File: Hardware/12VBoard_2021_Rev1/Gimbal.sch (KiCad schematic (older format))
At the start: 33 parts, among them Q6 CSD18537NQ5A, Q7 CSD18531Q5A, Q8 IRLML2060, U12 LM5116, U13 INA198, U3 LT1910

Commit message: found Big inductors
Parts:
- L8: value 6.8uH 1.5m -> 10uH; footprint MRDT_12VoltBoard:IND_SER2915L-682KL -> Inductor_THT:L_Radial_D27.9mm_P20.07mm_Vishay_IHB-3
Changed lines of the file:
@@
 AR Path="/5F74F36B/5FB68F3E/5FB7D727" Ref="L?"  Part="1"
 F 0 "L8" V 1600 3450 50  0000 C CNN
-F 1 "6.8uH 1.5m" V 1500 3450 50  0000 C CNN
-F 2 "MRDT_12VoltBoard:IND_SER2915L-682KL" H 1450 3550 50  0001 C CNN
+F 1 "10uH" V 1500 3450 50  0000 C CNN
+F 2 "Inductor_THT:L_Radial_D27.9mm_P20.07mm_Vishay_IHB-3" H 1450 3550 50  0001 C CNN
 F 3 "~" H 1450 3550 50  0001 C CNN
 	1    1450 3550

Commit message: Added all logic circuits for high current
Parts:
- R33: footprint Resistor_SMD:R_2512_6332Metric_Pad1.52x3.35mm_HandSolder -> Package_TO_SOT_THT:TO-126-2_Vertical
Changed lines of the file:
@@
 F 0 "R33" V 3193 3550 50  0000 C CNN
 F 1 "50m" V 3284 3550 50  0000 C CNN
-F 2 "Resistor_SMD:R_2512_6332Metric_Pad1.52x3.35mm_HandSolder" V 3330 3550 50  0001 C CNN
+F 2 "Package_TO_SOT_THT:TO-126-2_Vertical" V 3330 3550 50  0001 C CNN
 F 3 "~" H 3400 3550 50  0001 C CNN
 	1    3400 3550

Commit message: changed to big bucks
changed to the bucks used in Master due to a realization in the inductor sizing for the LM5116. It would be much bigger than previous years.
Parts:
- removed C33, C36: 100nF, Capacitor_SMD:C_0603_1608Metric_Pad1.05x0.95mm_HandSolder, symbol Device:C_Small
- removed C34: 2.2uF, Capacitor_SMD:C_0603_1608Metric_Pad1.05x0.95mm_HandSolder, symbol Device:C_Small
- removed C35: 1uF, Capacitor_SMD:C_0603_1608Metric_Pad1.05x0.95mm_HandSolder, symbol Device:C_Small
- removed C37, C40: 100uF, Capacitor_THT:CP_Radial_D6.3mm_P2.50mm, symbol Device:CP1_Small
- removed C38: 10pF, Capacitor_SMD:C_0603_1608Metric_Pad1.05x0.95mm_HandSolder, symbol Device:C_Small
- removed C39: 120pF, Capacitor_SMD:C_0603_1608Metric_Pad1.05x0.95mm_HandSolder, symbol Device:C_Small
- removed C41: 470pF, Capacitor_SMD:C_0603_1608Metric_Pad1.05x0.95mm_HandSolder, symbol Device:C_Small
- removed C42: 33nF, Capacitor_SMD:C_0603_1608Metric_Pad1.05x0.95mm_HandSolder, symbol Device:C_Small
- removed D17: 1.25V 250mA, Diode_SMD:D_SOD-323_HandSoldering, symbol Device:D_Small
- removed L8: 10uH, Inductor_THT:L_Radial_D27.9mm_P20.07mm_Vishay_IHB-3, symbol Device:L_Small
- removed Q6: CSD18537NQ5A, Package_SON:VSONP-8-1EP_5x6_P1.27mm, symbol 12VBoard_2021_Rev1-rescue:CSD18537NQ5A
- removed Q7: CSD18531Q5A, Package_SON:VSONP-8-1EP_5x6_P1.27mm, symbol 12VBoard_2021_Rev1-rescue:CSD18531Q5A
- removed R27: 5m, Resistor_SMD:R_0603_1608Metric_Pad1.05x0.95mm_HandSolder, symbol Device:R_Small
- removed R28: 36.5K, Resistor_SMD:R_0603_1608Metric_Pad1.05x0.95mm_HandSolder, symbol Device:R_Small
- removed R29: 2.26K, Resistor_SMD:R_0603_1608Metric_Pad1.05x0.95mm_HandSolder, symbol Device:R_Small
- removed R30: 86.6K, Resistor_SMD:R_0603_1608Metric_Pad1.05x0.95mm_HandSolder, symbol Device:R_Small
- removed R31: 9.76k, Resistor_SMD:R_0603_1608Metric_Pad1.05x0.95mm_HandSolder, symbol Device:R_Small
- removed R32: 261K, Resistor_SMD:R_0603_1608Metric_Pad1.05x0.95mm_HandSolder, symbol Device:R_Small
- removed U12: LM5116, Package_SO:TSSOP-20_4.4x6.5mm_P0.65mm, symbol 12VBoard_2021_Rev1-rescue:LM5116
- added C?: 0.1uF, Capacitor_SMD:C_0603_1608Metric_Pad1.05x0.95mm_HandSolder, symbol Device:C_Small
- added C?: 10uF, Capacitor_THT:CP_Radial_D5.0mm_P2.00mm, symbol Device:CP1_Small
- added R?: 0.01, Resistor_SMD:R_0603_1608Metric_Pad1.05x0.95mm_HandSolder, symbol Device:R
- added R?: 5.1K, Resistor_SMD:R_0603_1608Metric_Pad1.05x0.95mm_HandSolder, symbol Device:R
- added U?: LT1910, Package_SO:SOIC-8-N7_3.9x4.9mm_P1.27mm, symbol MRDT_ICs:LT1910
- added U?: FDS66900AS, symbol 12VBoard_2021_Rev1:FDS66900AS
- F3: value 5AMP -> 5A
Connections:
- net labels added: 12Actuation, 12V5AON
- net labels removed: AGNDPGND, COMPFB, CS, CSGDEMB, HB, HO, LO, PackVoltage, SW, VCC, VOUTVCCX
- wire segments 167 -> 81
- no-connect marks 1 -> 0
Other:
- moved on the sheet: D18, F3, R33, R34, TP7, U13

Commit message: Started work on updated layout
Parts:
- added D15: Aux Mount Acuation Gree, Diode_SMD:D_0603_1608Metric_Pad1.05x0.95mm_HandSolder, symbol Device:LED
- added R22: 1.2k, Resistor_SMD:R_0603_1608Metric_Pad1.05x0.95mm_HandSolder, symbol Device:R
- U18: renamed from U?; footprint (none) -> Package_SO:SOIC-8_3.9x4.9mm_P1.27mm
- gave numbers to parts that had none: 5
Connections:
- wire segments 81 -> 82
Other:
- note removed: "Green"
- moved on the sheet: D18, R34
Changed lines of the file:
@@
 $EndDescr
-$Comp
-L Device:R R?
-U 1 1 5F98969B
-P 3975 2950
-AR Path="/5F74F36B/5F821EB2/5F98969B" Ref="R?"  Part="1"
-AR Path="/5F74F36B/5F8222BE/5F98969B" Ref="R?"  Part="1"
-AR Path="/5F74F36B/5F971CD6/5F98969B" Ref="R34"  Part="1"
-AR Path="/5F74F36B/5FB68F3E/5F98969B" Ref="R?"  Part="1"
-F 0 "R34" H 4025 2950 50  0000 L CNN
-F 1 "1.2k" V 3975 2880 39  0000 L CNN
-F 2 "Resistor_SMD:R_0603_1608Metric_Pad1.05x0.95mm_HandSolder" V 3905 2950 50  0001 C CNN
-F 3 "~" H 3975 2950 50  0001 C CNN
-	1    3975 2950
-	1    0    0    -1
-$EndComp
-$Comp
-L power:GND #PWR?
-U 1 1 5F9896A1
-P 3975 3600
-AR Path="/5F74F36B/5F821EB2/5F9896A1" Ref="#PWR?"  Part="1"
-AR Path="/5F74F36B/5F8222BE/5F9896A1" Ref="#PWR?"  Part="1"
-AR Path="/5F74F36B/5F971CD6/5F9896A1" Ref="#PWR078"  Part="1"
-AR Path="/5F74F36B/5FB68F3E/5F9896A1" Ref="#PWR?"  Part="1"
-F 0 "#PWR078" H 3975 3350 50  0001 C CNN
-F 1 "GND" H 3980 3427 50  0000 C CNN
-F 2 "" H 3975 3600 50  0001 C CNN
-F 3 "" H 3975 3600 50  0001 C CNN
-	1    3975 3600
-	1    0    0    -1
-$EndComp
-$Comp
-L Device:LED D?
-U 1 1 5F9896A7
-P 3975 3350
-AR Path="/5F74F36B/5F821EB2/5F9896A7" Ref="D?"  Part="1"
-AR Path="/5F74F36B/5F8222BE/5F9896A7" Ref="D?"  Part="1"
-AR Path="/5F74F36B/5F971CD6/5F9896A7" Ref="D18"  Part="1"
-AR Path="/5F74F36B/5FB68F3E/5F9896A7" Ref="D?"  Part="1"
-F 0 "D18" V 4014 3233 50  0000 R CNN
-F 1 "Gimbal Acuation Gree" V 3923 3233 50  0000 R CNN
-F 2 "Diode_SMD:D_0603_1608Metric_Pad1.05x0.95mm_HandSolder" H 3975 3350 50  0001 C CNN
-F 3 "~" H 3975 3350 50  0001 C CNN
-	1    3975 3350
-	0    -1   -1   0
-$EndComp
-Wire Wire Line
-	3975 3600 3975 3500
-Wire Wire Line
-	3975 3200 3975 3100
-Wire Wire Line
-	3975 2800 3975 2750
-Connection ~ 3975 2750
-Wire Wire Line
-	3975 2750 4375 2750
-Text Notes 4025 2850 0    50   ~ 0
-Green
 $Comp
 L Amplifier_Current:INA198 U?
@@
 GimbalCTL_Act
 $Comp
-L MRDT_ICs:LT1910 U?
+L MRDT_ICs:LT1910 U12
 U 1 1 605C691C
 P 2900 1775
-F 0 "U?" H 3275 2462 60  0000 C CNN
+F 0 "U12" H 3275 2462 60  0000 C CNN
 F 1 "LT1910" H 3275 2356 60  0000 C CNN
 F 2 "Package_SO:SOIC-8-N7_3.9x4.9mm_P1.27mm" H 2900 1775 60  0001 C CNN
@@
 $EndComp
 $Comp
-L Device:C_Small C?
+L Device:C_Small C15
 U 1 1 605C6922
 P 2625 1850
-F 0 "C?" H 2717 1896 50  0000 L CNN
+F 0 "C15" H 2717 1896 50  0000 L CNN
 F 1 "0.1uF" H 2717 1805 50  0000 L CNN
 F 2 "Capacitor_SMD:C_0603_1608Metric_Pad1.05x0.95mm_HandSolder" H 2625 1850 50  0001 C CNN
@@
 $EndComp
 $Comp
-L Device:CP1_Small C?
+L Device:CP1_Small C16
 U 1 1 605C6928
 P 3950 1850
-F 0 "C?" H 3775 1900 50  0000 L CNN
+F 0 "C16" H 3775 1900 50  0000 L CNN
 F 1 "10uF" H 3725 1775 50  0000 L CNN
 F 2 "Capacitor_THT:CP_Radial_D5.0mm_P2.00mm" H 3950 1850 50  0001 C CNN
@@
 $EndComp
 $Comp
-L power:GND #PWR?
+L power:GND #PWR0112
 U 1 1 605C692E
 P 3300 2025
-F 0 "#PWR?" H 3300 1775 50  0001 C CNN
+F 0 "#PWR0112" H 3300 1775 50  0001 C CNN
 F 1 "GND" H 3305 1852 50  0000 C CNN
 F 2 "" H 3300 2025 50  0001 C CNN
@@
 	2600 1525 2700 1525
 $Comp
-L Device:R R?
+L Device:R R17
 U 1 1 605C6959
 P 4100 1300
-F 0 "R?" H 4145 1305 50  0000 L CNN
+F 0 "R17" H 4145 1305 50  0000 L CNN
 F 1 "0.01" V 4100 1225 50  0000 L CNN
 F 2 "Resistor_SMD:R_0603_1608Metric_Pad1.05x0.95mm_HandSolder" V 4030 1300 50  0001 C CNN
@@
 $EndComp
 $Comp
-L Device:R R?
+L Device:R R13
 U 1 1 605C695F
 P 2500 1375
-F 0 "R?" V 2420 1375 50  0000 C CNN
+F 0 "R13" V 2420 1375 50  0000 C CNN
 F 1 "5.1K" V 2500 1375 39  0000 C CNN
 F 2 "Resistor_SMD:R_0603_1608Metric_Pad1.05x0.95mm_HandSolder" V 2430 1375 50  0001 C CNN
@@
 U 1 1 60619542
 P 4850 1825
-F 0 "U?" H 4850 2240 50  0000 C CNN
+AR Path="/60619542" Ref="U?"  Part="1"
+AR Path="/5F74F36B/5F971CD6/60619542" Ref="U18"  Part="1"
+F 0 "U18" H 4850 2240 50  0000 C CNN
 F 1 "FDS66900AS" H 4850 2149 50  0000 C CNN
-F 2 "" H 4900 1975 50  0001 C CNN
+F 2 "Package_SO:SOIC-8_3.9x4.9mm_P1.27mm" H 4900 1975 50  0001 C CNN
 F 3 "" H 4900 1975 50  0001 C CNN
 	1    4850 1825
@@
 	2925 2750 2675 2750
 Connection ~ 2925 2750
-Wire Wire Line
-	3925 2750 3975 2750
 $Comp
 L Device:Fuse F?
@@
 	0    1    1    0
 $EndComp
+$Comp
+L Device:R R?
+U 1 1 5FD693BE
+P 8025 2225
+AR Path="/5F74F36B/5F821EB2/5FD693BE" Ref="R?"  Part="1"
+AR Path="/5F74F36B/5F8222BE/5FD693BE" Ref="R?"  Part="1"
+AR Path="/5F74F36B/5F971CD6/5FD693BE" Ref="R22"  Part="1"
+AR Path="/5F74F36B/5FB68F3E/5FD693BE" Ref="R?"  Part="1"
+F 0 "R22" H 8075 2225 50  0000 L CNN
+F 1 "1.2k" V 8025 2155 39  0000 L CNN
+F 2 "Resistor_SMD:R_0603_1608Metric_Pad1.05x0.95mm_HandSolder" V 7955 2225 50  0001 C CNN
+F 3 "~" H 8025 2225 50  0001 C CNN
+	1    8025 2225
+	1    0    0    -1
+$EndComp
+$Comp
+L power:GND #PWR?
+U 1 1 5FD693C4
+P 8025 2875
+AR Path="/5F74F36B/5F821EB2/5FD693C4" Ref="#PWR?"  Part="1"
+AR Path="/5F74F36B/5F8222BE/5FD693C4" Ref="#PWR?"  Part="1"
+AR Path="/5F74F36B/5F971CD6/5FD693C4" Ref="#PWR08"  Part="1"
+AR Path="/5F74F36B/5FB68F3E/5FD693C4" Ref="#PWR?"  Part="1"
+F 0 "#PWR08" H 8025 2625 50  0001 C CNN
+F 1 "GND" H 8030 2702 50  0000 C CNN
+F 2 "" H 8025 2875 50  0001 C CNN
+F 3 "" H 8025 2875 50  0001 C CNN
+	1    8025 2875
+	1    0    0    -1
+$EndComp
+$Comp
+L Device:LED D?
+U 1 1 5FD693CA
+P 8025 2625
+AR Path="/5F74F36B/5F821EB2/5FD693CA" Ref="D?"  Part="1"
+AR Path="/5F74F36B/5F8222BE/5FD693CA" Ref="D?"  Part="1"
+AR Path="/5F74F36B/5F971CD6/5FD693CA" Ref="D15"  Part="1"
+AR Path="/5F74F36B/5FB68F3E/5FD693CA" Ref="D?"  Part="1"
+F 0 "D15" V 8064 2508 50  0000 R CNN
+F 1 "Aux Mount Acuation Gree" V 7973 2508 50  0000 R CNN
+F 2 "Diode_SMD:D_0603_1608Metric_Pad1.05x0.95mm_HandSolder" H 8025 2625 50  0001 C CNN
+F 3 "~" H 8025 2625 50  0001 C CNN
+	1    8025 2625
+	0    -1   -1   0
+$EndComp
+Wire Wire Line
+	8025 2875 8025 2775
+Wire Wire Line
+	8025 2475 8025 2375
+Wire Wire Line
+	8025 2000 8025 2075
+Connection ~ 8025 2000
+Wire Wire Line
+	5375 2500 5375 2400
+Wire Wire Line
+	5375 2900 5375 2800
+$Comp
+L Device:LED D?
+U 1 1 5F9896A7
+P 5375 2650
+AR Path="/5F74F36B/5F821EB2/5F9896A7" Ref="D?"  Part="1"
+AR Path="/5F74F36B/5F8222BE/5F9896A7" Ref="D?"  Part="1"
+AR Path="/5F74F36B/5F971CD6/5F9896A7" Ref="D18"  Part="1"
+AR Path="/5F74F36B/5FB68F3E/5F9896A7" Ref="D?"  Part="1"
+F 0 "D18" V 5414 2533 50  0000 R CNN
+F 1 "Gimbal Acuation Gree" V 5323 2533 50  0000 R CNN
+F 2 "Diode_SMD:D_0603_1608Metric_Pad1.05x0.95mm_HandSolder" H 5375 2650 50  0001 C CNN
+F 3 "~" H 5375 2650 50  0001 C CNN
+	1    5375 2650
+	0    -1   -1   0
+$EndComp
+$Comp
+L power:GND #PWR?
+U 1 1 5F9896A1
+P 5375 2900
+AR Path="/5F74F36B/5F821EB2/5F9896A1" Ref="#PWR?"  Part="1"
+AR Path="/5F74F36B/5F8222BE/5F9896A1" Ref="#PWR?"  Part="1"
+AR Path="/5F74F36B/5F971CD6/5F9896A1" Ref="#PWR078"  Part="1"
+AR Path="/5F74F36B/5FB68F3E/5F9896A1" Ref="#PWR?"  Part="1"
+F 0 "#PWR078" H 5375 2650 50  0001 C CNN
+F 1 "GND" H 5380 2727 50  0000 C CNN
+F 2 "" H 5375 2900 50  0001 C CNN
+F 3 "" H 5375 2900 50  0001 C CNN
+	1    5375 2900
+	1    0    0    -1
+$EndComp
+$Comp
+L Device:R R?
+U 1 1 5F98969B
+P 5375 2250
+AR Path="/5F74F36B/5F821EB2/5F98969B" Ref="R?"  Part="1"
+AR Path="/5F74F36B/5F8222BE/5F98969B" Ref="R?"  Part="1"
+AR Path="/5F74F36B/5F971CD6/5F98969B" Ref="R34"  Part="1"
+AR Path="/5F74F36B/5FB68F3E/5F98969B" Ref="R?"  Part="1"
+F 0 "R34" H 5425 2250 50  0000 L CNN
+F 1 "1.2k" V 5375 2180 39  0000 L CNN
+F 2 "Resistor_SMD:R_0603_1608Metric_Pad1.05x0.95mm_HandSolder" V 5305 2250 50  0001 C CNN
+F 3 "~" H 5375 2250 50  0001 C CNN
+	1    5375 2250
+	1    0    0    -1
+$EndComp
+Connection ~ 5375 2100
+Wire Wire Line
+	3925 2750 4375 2750
 $EndSCHEMATC

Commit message: Layout for high current
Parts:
- U18: symbol 12VBoard_2021_Rev1:FDS66900AS -> 12VBoard_2021_Rev1-rescue:FDS66900AS-12VBoard_2021_Rev1
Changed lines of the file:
@@
 	4100 1450 4100 1525
 $Comp
-L 12VBoard_2021_Rev1:FDS66900AS U?
+L 12VBoard_2021_Rev1-rescue:FDS66900AS-12VBoard_2021_Rev1 U?
 U 1 1 60619542
 P 4850 1825

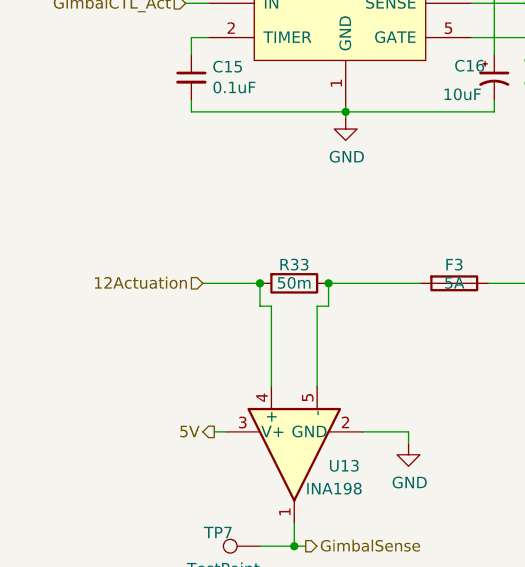
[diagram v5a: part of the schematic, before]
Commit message: fisnished board traces
still a problem with 12VAcuation
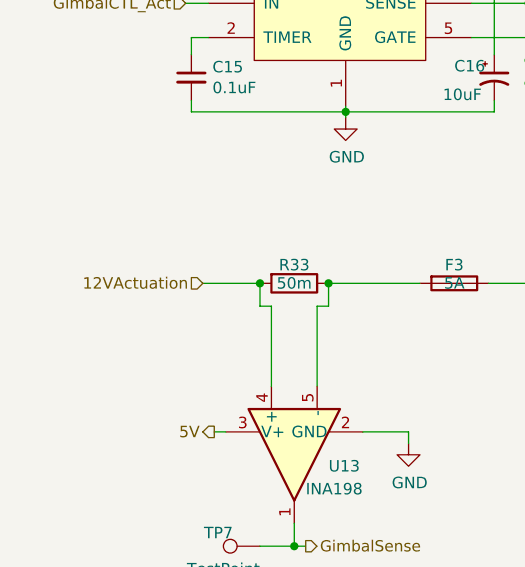
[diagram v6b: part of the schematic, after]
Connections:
- net 12Actuation renamed 12VActuation
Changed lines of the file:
@@
 Connection ~ 3225 2750
 Text HLabel 2675 2750 0    50   Input ~ 0
-12Actuation
+12VActuation
 Text HLabel 5400 2100 2    50   Input ~ 0
 12V5AGimbal

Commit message: Started work on BOM
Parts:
- R33: footprint Package_TO_SOT_THT:TO-126-2_Vertical -> Resistor_SMD:R_2010_5025Metric_Pad1.52x2.65mm_HandSolder
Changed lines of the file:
@@
 EESchema Schematic File Version 4
-LIBS:12VBoard_2021_Rev1-cache
 EELAYER 30 0
 EELAYER END
@@
 F 0 "R33" V 2995 2750 50  0000 C CNN
 F 1 "50m" V 3075 2750 50  0000 C CNN
-F 2 "Package_TO_SOT_THT:TO-126-2_Vertical" V 3005 2750 50  0001 C CNN
+F 2 "Resistor_SMD:R_2010_5025Metric_Pad1.52x2.65mm_HandSolder" V 3005 2750 50  0001 C CNN
 F 3 "~" H 3075 2750 50  0001 C CNN
 	1    3075 2750
